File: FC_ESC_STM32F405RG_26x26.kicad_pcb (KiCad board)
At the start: 2 copper layers, 30.5 x 30.5 mm, 220 parts, among them J1 Conn_02x03_Odd_Even, J10 I2C2_UART3, J11 SD CARD, J12 UART1, J13 UART6, J14 UART4, J15 PWM, J16 MOTOR, J17 OSD, J18 Conn_01x02, J19 LED_STRIP, J2 USB_A, J20 ESC_PROG, J21 ALARM, J3 Debugger, J4 RC, J5 MOTOR, J6 MOTOR, J7 MOTOR, J8 VOL_CUR, J9 RSSI, Q1 FDS6912, Q10 FDS6912, Q11 FDS6912, Q13 FDS6912, Q2 FDS6912, Q3 FDS6912, Q4 FDS6912, Q5 FDS6912, Q6 FDS6912, Q7 FDS6912, Q8 FDS6912, Q9 FDS6912, SW1 RST, U1 TPS62822DLC, U10 EFM8BB21, U11 FD6288Q, U12 BMP280, U13 MPU-6000, U14 LM358, U15 outline, U2 TPS54560BDDA, U3 EFM8BB21, U4 FD6288Q, U5 STM32F405RGTx, U6 EFM8BB21, U7 FD6288Q, U8 EFM8BB21, U9 FD6288Q, Y1 8MHz

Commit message: update placement
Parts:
- removed Q13: FDS6912, Package_SO:SOIC-8_3.9x4.9mm_P1.27mm
- added Q12: SIZ200, Proj_footprint:ONSC-WDFN-8-511AB_V, B.Cu at (214.1, 70.3)
- C1: renamed from C11; moved to B.Cu
- C10: renamed from C38; moved to B.Cu
- C11: renamed from C28; moved to B.Cu
- C12: renamed from C39; moved to B.Cu
- C16: renamed from C13; moved to B.Cu
- C17: renamed from C40; moved to B.Cu
- C18: renamed from C16; moved to B.Cu
- C19: renamed from C41; moved to B.Cu
- C2: renamed from C36; moved to B.Cu
- C21: renamed from C17; moved to B.Cu
- C22: renamed from C42; moved to B.Cu
- C23: renamed from C29; moved to B.Cu
- C24: renamed from C43; moved to B.Cu
- C25: renamed from C30; moved to B.Cu
- C26: renamed from C44; moved to B.Cu
- C29: renamed from C31; moved to B.Cu
- C3: renamed from C12; moved to B.Cu
- C30: renamed from C45; moved to B.Cu
- C31: renamed from C32; moved to B.Cu
- C32: renamed from C46; moved to B.Cu
- C33, U4: moved to B.Cu
- C34: renamed from C47; moved to B.Cu
- C35: renamed from C34; moved to B.Cu
- C36: renamed from C48; moved to B.Cu
- C37: renamed from C35; moved to B.Cu
- C38: renamed from C49; moved to B.Cu
- C4: renamed from C37; moved to B.Cu
- C9: renamed from C27; moved to B.Cu
- D12: renamed from D3; footprint Package_TO_SOT_SMD:SOT-23-3 -> Diode_SMD:D_SOD-123F; moved to B.Cu
- D13: renamed from D11; footprint Package_TO_SOT_SMD:SOT-23-3 -> Diode_SMD:D_SOD-123F; moved to B.Cu
- D14: renamed from D4; footprint Package_TO_SOT_SMD:SOT-23-3 -> Diode_SMD:D_SOD-123F; moved to B.Cu
- D15: renamed from D12; footprint Package_TO_SOT_SMD:SOT-23-3 -> Diode_SMD:D_SOD-123F; moved to B.Cu
- D16: renamed from D7; footprint Package_TO_SOT_SMD:SOT-23-3 -> Diode_SMD:D_SOD-123F; moved to B.Cu
- D17: renamed from D13; footprint Package_TO_SOT_SMD:SOT-23-3 -> Diode_SMD:D_SOD-123F; moved to B.Cu
- D2: footprint Package_TO_SOT_SMD:SOT-23-3 -> Diode_SMD:D_SOD-123F; moved to B.Cu
- D3: renamed from D8; footprint Package_TO_SOT_SMD:SOT-23-3 -> Diode_SMD:D_SOD-123F; moved to B.Cu
- D6: renamed from D5; footprint Package_TO_SOT_SMD:SOT-23-3 -> Diode_SMD:D_SOD-123F; moved to B.Cu
- D7: renamed from D9; footprint Package_TO_SOT_SMD:SOT-23-3 -> Diode_SMD:D_SOD-123F; moved to B.Cu
- D8: renamed from D6; footprint Package_TO_SOT_SMD:SOT-23-3 -> Diode_SMD:D_SOD-123F; moved to B.Cu
- D9: renamed from D10; footprint Package_TO_SOT_SMD:SOT-23-3 -> Diode_SMD:D_SOD-123F; moved to B.Cu
- L1: footprint Inductor_SMD:L_Bourns_SRP1038C_10.0x10.0mm -> Inductor_SMD:L_Chilisin_BMRA00040420
- Q1, Q10, Q11, Q2, Q3, Q4, Q5, Q6, Q7, Q8, Q9: value FDS6912 -> SIZ200; footprint Package_SO:SOIC-8_3.9x4.9mm_P1.27mm -> Proj_footprint:ONSC-WDFN-8-511AB_V; moved to B.Cu
- R1: renamed from R8; moved to B.Cu
- R10: renamed from R23; moved to B.Cu
- R11: renamed from R47; moved to B.Cu
- R12: renamed from R48; moved to B.Cu
- R13: renamed from R24; moved to B.Cu
- R14: renamed from R49; moved to B.Cu
- R17: renamed from R12; moved to B.Cu
- R18: renamed from R13; moved to B.Cu
- R19: renamed from R50; moved to B.Cu
- R2: renamed from R43; moved to B.Cu
- R20: renamed from R51; moved to B.Cu
- R21: renamed from R19; moved to B.Cu
- R22: renamed from R20; moved to B.Cu
- R23: renamed from R52; moved to B.Cu
- R24: renamed from R53; moved to B.Cu
- R25: renamed from R21; moved to B.Cu
- R26: renamed from R54; moved to B.Cu
- R29: renamed from R14; moved to B.Cu
- R3: renamed from R9; moved to B.Cu
- R30: renamed from R15; moved to B.Cu
- R31: renamed from R55; moved to B.Cu
- R32: renamed from R56; moved to B.Cu
- R33: renamed from R18; moved to B.Cu
- R34: renamed from R16; moved to B.Cu
- R35: renamed from R57; moved to B.Cu
- R36: renamed from R58; moved to B.Cu
- R37: renamed from R17; moved to B.Cu
- R38: renamed from R59; moved to B.Cu
- R4: renamed from R10; moved to B.Cu
- R40: renamed from R26; moved to B.Cu
- R41: renamed from R60; moved to B.Cu
- R42: renamed from R27; moved to B.Cu
- R43: renamed from R28; moved to B.Cu
- R44: renamed from R29; moved to B.Cu
- R45: renamed from R61; moved to B.Cu
- R46: renamed from R62; moved to B.Cu
- R47: renamed from R63; moved to B.Cu
- R48: renamed from R30; moved to B.Cu
- R49: renamed from R31; moved to B.Cu
- R5: renamed from R11; moved to B.Cu
- R50: renamed from R64; moved to B.Cu
- R51: renamed from R65; moved to B.Cu
- R54: renamed from R32; moved to B.Cu
- R55: renamed from R66; moved to B.Cu
- R56: renamed from R33; moved to B.Cu
- R57: renamed from R34; moved to B.Cu
- R58: renamed from R67; moved to B.Cu
- R59: renamed from R68; moved to B.Cu
- R6: renamed from R44; moved to B.Cu
- R60: renamed from R35; moved to B.Cu
- R61: renamed from R36; moved to B.Cu
- R62: renamed from R69; moved to B.Cu
- R63: renamed from R70; moved to B.Cu
- R64: renamed from R37; moved to B.Cu
- R65: renamed from R71; moved to B.Cu
- R66: renamed from R38; moved to B.Cu
- R67: renamed from R39; moved to B.Cu
- R68: renamed from R72; moved to B.Cu
- R69: renamed from R73; moved to B.Cu
- R7: renamed from R45; moved to B.Cu
- R70: renamed from R40; moved to B.Cu
- R71: renamed from R41; moved to B.Cu
- R72: renamed from R74; moved to B.Cu
- R73: renamed from R75; moved to B.Cu
- R74: renamed from R42; moved to B.Cu
- R75: renamed from R76; moved to B.Cu
- R8: renamed from R46; moved to B.Cu
- R9: renamed from R22; moved to B.Cu
- U1: renamed from U3; moved to B.Cu
- U10: renamed from U11; moved to B.Cu
- U2: renamed from U8; moved to B.Cu
- U5: renamed from U9; moved to B.Cu
- U7: renamed from U6; moved to B.Cu
- U8: renamed from U10; moved to B.Cu
- U9: renamed from U7; moved to B.Cu
- Y1: footprint Crystal:Crystal_SMD_5032-4Pin_5.0x3.2mm -> Crystal:Crystal_SMD_3225-4Pin_3.2x2.5mm
- moved C16 282.4 mm to (279.4, 52.7), turned to 180 degrees
- moved C18 282.4 mm to (279.4, 60.2), turned to 180 degrees
- moved C21 282.4 mm to (279.4, 62.7), turned to 180 degrees
- moved C3 282.4 mm to (279.4, 50.1), turned to 180 degrees
- moved C11 274.4 mm to (275.4, 50.1), turned to 180 degrees
- moved R1 258.4 mm to (267.4, 52.7), turned to 180 degrees
- moved R17 258.4 mm to (267.4, 62.7), turned to 180 degrees
- moved R18 258.4 mm to (267.4, 65.2), turned to 180 degrees
- moved R29 258.4 mm to (267.4, 67.7), turned to 180 degrees
- moved R3 258.4 mm to (267.4, 55.2), turned to 180 degrees
- moved R30 258.4 mm to (267.4, 70.2), turned to 180 degrees
- moved R34 258.4 mm to (267.4, 72.7), turned to 180 degrees
- moved R37 258.4 mm to (267.4, 75.2), turned to 180 degrees
- moved R10 250.4 mm to (263.4, 52.7), turned to 180 degrees
- moved R13 250.4 mm to (263.4, 55.2), turned to 180 degrees
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- renumbered C5 to C13, C6 to C14, C7 to C15, C8 to C20, C9 to C27, C10 to C28, C52 to C39, C50 to C40, C54 to C41, C53 to C42, C26 to C43, C24 to C44, C25 to C45, C23 to C46, C22 to C47, C14 to C48, C15 to C49, C2 to C5, C18 to C50, C19 to C52, C57 to C53, C55 to C54, C56 to C55, C20 to C56, C21 to C57, C1 to C6, C3 to C7, C4 to C8, D17 to D10, D16 to D11, D14 to D4, D15 to D5, J18 to J1, J14 to J10, J15 to J11, J17 to J12, J21 to J13, J19 to J14, J4 to J15, J7 to J16, J5 to J17, J6 to J18, J16 to J19, J20 to J2, J2 to J20, J1 to J21, J8 to J4, J9 to J5, J10 to J6, J11 to J7, J12 to J8, J13 to J9, JP4 to JP1, JP1 to JP2, JP2 to JP3, JP3 to JP4, R1 to R15, R2 to R16, R3 to R27, R4 to R28, R5 to R39, R6 to R52, R7 to R53, R79 to R76, R85 to R77, R86 to R78, R77 to R79, R84 to R80, R83 to R81, R25 to R83, R78 to R84, R87 to R85, R80 to R86, R88 to R87, R89 to R88, R81 to R89, U15 to U11, U13 to U12, U12 to U13, U5 to U15, U2 to U3, U1 to U6
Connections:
- C44 pad 1: Net-(U5-PH0) -> Net-(U15-PH0)
- C45 pad 1: Net-(U5-PH1) -> Net-(U15-PH1)
- Q1 pad 2: Net-(Q1A-G1) -> Net-(Q1-G2)
- Q1 pad 3: ESC1_VS2 -> ESC1_VS1
- Q1 pad 4: Net-(Q1B-G2) -> Net-(Q1-G1)
- Q1 pad 6: V_BAT -> (no net)
- Q1 pad 7: ESC1_VS2 -> (no net)
- Q1 pad 8: ESC1_VS2 -> (no net)
- Q10 pad 6: V_BAT -> (no net)
- Q10 pad 7: ESC4_VS2 -> (no net)
- Q10 pad 8: ESC4_VS2 -> (no net)
- Q11 pad 2: Net-(Q11A-G1) -> Net-(Q11-G2)
- Q11 pad 3: ESC4_VS3 -> ESC2_VS3
- Q11 pad 4: Net-(Q11B-G2) -> Net-(Q11-G1)
- Q11 pad 6: V_BAT -> (no net)
- Q11 pad 7: ESC4_VS3 -> (no net)
- Q11 pad 8: ESC4_VS3 -> (no net)
- Q2 pad 2: Net-(Q2A-G1) -> Net-(Q2-G2)
- Q2 pad 3: ESC1_VS3 -> ESC3_VS1
- Q2 pad 4: Net-(Q2B-G2) -> Net-(Q2-G1)
- Q2 pad 6: V_BAT -> (no net)
- Q2 pad 7: ESC1_VS3 -> (no net)
- Q2 pad 8: ESC1_VS3 -> (no net)
- Q3 pad 2: Net-(Q3A-G1) -> Net-(Q3-G2)
- Q3 pad 3: ESC2_VS1 -> ESC1_VS2
- Q3 pad 4: Net-(Q3B-G2) -> Net-(Q3-G1)
- Q3 pad 6: V_BAT -> (no net)
- Q3 pad 7: ESC2_VS1 -> (no net)
- Q3 pad 8: ESC2_VS1 -> (no net)
- Q4 pad 2: Net-(Q4A-G1) -> Net-(Q4-G2)
- Q4 pad 3: ESC2_VS2 -> ESC3_VS2
- Q4 pad 4: Net-(Q4B-G2) -> Net-(Q4-G1)
- Q4 pad 6: V_BAT -> (no net)
- Q4 pad 7: ESC2_VS2 -> (no net)
- Q4 pad 8: ESC2_VS2 -> (no net)
- Q5 pad 2: Net-(Q5A-G1) -> Net-(Q5-G2)
- Q5 pad 3: ESC2_VS3 -> ESC1_VS3
- Q5 pad 4: Net-(Q5B-G2) -> Net-(Q5-G1)
- Q5 pad 6: V_BAT -> (no net)
- Q5 pad 7: ESC2_VS3 -> (no net)
- Q5 pad 8: ESC2_VS3 -> (no net)
- Q6 pad 2: Net-(Q6A-G1) -> Net-(Q6-G2)
- Q6 pad 3: ESC3_VS1 -> ESC3_VS3
- Q6 pad 4: Net-(Q6B-G2) -> Net-(Q6-G1)
- Q6 pad 6: V_BAT -> (no net)
- Q6 pad 7: ESC3_VS1 -> (no net)
- Q6 pad 8: ESC3_VS1 -> (no net)
- Q7 pad 2: Net-(Q7A-G1) -> Net-(Q7-G2)
- Q7 pad 3: ESC3_VS2 -> ESC2_VS1
- Q7 pad 4: Net-(Q7B-G2) -> Net-(Q7-G1)
- Q7 pad 6: V_BAT -> (no net)
- Q7 pad 7: ESC3_VS2 -> (no net)
- Q7 pad 8: ESC3_VS2 -> (no net)
- Q8 pad 2: Net-(Q8A-G1) -> Net-(Q8-G2)
- Q8 pad 3: ESC3_VS3 -> ESC4_VS1
- Q8 pad 4: Net-(Q8B-G2) -> Net-(Q8-G1)
- Q8 pad 6: V_BAT -> (no net)
- Q8 pad 7: ESC3_VS3 -> (no net)
- Q8 pad 8: ESC3_VS3 -> (no net)
- Q9 pad 2: Net-(Q9A-G1) -> Net-(Q9-G2)
- Q9 pad 3: ESC4_VS1 -> ESC2_VS2
- Q9 pad 4: Net-(Q9B-G2) -> Net-(Q9-G1)
- Q9 pad 6: V_BAT -> (no net)
- Q9 pad 7: ESC4_VS1 -> (no net)
- Q9 pad 8: ESC4_VS1 -> (no net)
- R17 pad 2: Net-(Q1B-G2) -> Net-(Q3-G1)
- R18 pad 2: Net-(Q1A-G1) -> Net-(Q3-G2)
- R19 pad 2: Net-(Q7B-G2) -> Net-(Q4-G1)
- R20 pad 2: Net-(Q7A-G1) -> Net-(Q4-G2)
- R29 pad 2: Net-(Q2B-G2) -> Net-(Q5-G1)
- R30 pad 2: Net-(Q2A-G1) -> Net-(Q5-G2)
- R31 pad 2: Net-(Q8B-G2) -> Net-(Q6-G1)
- R32 pad 2: Net-(Q8A-G1) -> Net-(Q6-G2)
- R4 pad 2: Net-(Q13B-G2) -> Net-(Q1-G1)
- R43 pad 2: Net-(Q3B-G2) -> Net-(Q7-G1)
- R44 pad 2: Net-(Q3A-G1) -> Net-(Q7-G2)
- R46 pad 2: Net-(Q9B-G2) -> Net-(Q8-G1)
- R47 pad 2: Net-(Q9A-G1) -> Net-(Q8-G2)
- R5 pad 2: Net-(Q13A-G1) -> Net-(Q1-G2)
- R56 pad 2: Net-(Q4B-G2) -> Net-(Q9-G1)
- R57 pad 2: Net-(Q4A-G1) -> Net-(Q9-G2)
- R66 pad 2: Net-(Q5B-G2) -> Net-(Q11-G1)
- R67 pad 2: Net-(Q5A-G1) -> Net-(Q11-G2)
- R68 pad 2: Net-(Q11B-G2) -> Net-(Q12-G1)
- R69 pad 2: Net-(Q11A-G1) -> Net-(Q12-G2)
- R7 pad 2: Net-(Q6B-G2) -> Net-(Q2-G1)
- R8 pad 2: Net-(Q6A-G1) -> Net-(Q2-G2)
- U15 pad 5: Net-(U5-PH0) -> Net-(U15-PH0)
- U15 pad 6: Net-(U5-PH1) -> Net-(U15-PH1)
- Y1 pad 1: Net-(U5-PH0) -> Net-(U15-PH1)
- Y1 pad 2: Net-(U5-PH1) -> Net-(U15-PH0)
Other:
- board size 30.5 x 30.5 mm -> 34 x 34 mm

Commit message: update placement
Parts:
- C11, C12, C13, C16, C17, C18, C19, C21, C22, C25, C26, C27, C3, C31, C32, C33, C34, C35, C36, C37, C38, C39, C4, C40, C41, C42, C43, C44, C45, C46, C47, C48, C49, C50, C51, C52, C53, C54, C55, C56, C57, C7, C8: footprint Capacitor_SMD:C_0603_1608Metric -> Capacitor_SMD:C_0402_1005Metric_Pad0.74x0.62mm_HandSolder
- J16, J17, J18, J19: footprint Connector_PinSocket_1.27mm:PinSocket_1x03_P1.27mm_Vertical -> Proj_footprint:Hirose_DF13-03P-1.25DS_1x03_P1.25mm_Horizontal; moved to B.Cu
- R1, R10, R11, R12, R13, R14, R15, R16, R17, R18, R19, R2, R20, R21, R22, R23, R24, R25, R26, R27, R28, R29, R3, R30, R31, R32, R33, R34, R35, R36, R37, R38, R39, R4, R40, R41, R42, R43, R44, R45, R46, R47, R48, R49, R5, R50, R51, R52, R53, R54, R55, R56, R57, R58, R59, R6, R60, R61, R62, R63, R64, R65, R66, R67, R68, R69, R7, R70, R71, R72, R73, R74, R75, R76, R77, R78, R79, R8, R80, R81, R82, R83, R84, R85, R86, R87, R88, R89, R9: footprint Resistor_SMD:R_0603_1608Metric -> Resistor_SMD:R_0402_1005Metric_Pad0.72x0.64mm_HandSolder
- U1, U2, U7, U8: footprint Package_DFN_QFN:SiliconLabs_QFN-20-1EP_3x3mm_P0.5mm_EP1.8x1.8mm -> Proj_footprint:QFN-20-1EP_3x3mm_P0.5mm_EP1.8x1.8mm
- U12: footprint Package_DFN_QFN:QFN-24-1EP_4x4mm_P0.5mm_EP2.15x2.15mm -> Proj_footprint:QFN-24-1EP_4x4mm_P0.5mm_EP2.15x2.15mm
- moved R41 195.9 mm to (238.7, 65.5)
- moved R45 195.9 mm to (238.7, 68.0)
- moved R73 187.6 mm to (225.4, 66.7), turned to 90 degrees
- moved R75 186.7 mm to (224.6, 69.5), turned to 90 degrees
- moved R72 183.1 mm to (223.6, 69.5), turned to -90 degrees
- moved R69 180.8 mm to (222.6, 69.5), turned to 90 degrees
- moved R68 178.7 mm to (221.7, 69.5), turned to 90 degrees
- moved R63 176.6 mm to (220.6, 66.7), turned to 90 degrees
- moved R65 175.7 mm to (219.7, 69.5), turned to 90 degrees
- moved R46 175.0 mm to (212.0, 69.5), turned to 90 degrees
- moved R62 172.2 mm to (218.8, 69.5), turned to -90 degrees
- moved R59 170.0 mm to (217.8, 69.5), turned to 90 degrees
- moved R58 167.9 mm to (216.8, 69.5), turned to 90 degrees
- moved R51 165.9 mm to (215.8, 66.7), turned to 90 degrees
- moved R55 165.0 mm to (214.9, 69.5), turned to 90 degrees
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
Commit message: update placement
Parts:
- removed the C11 at (244.1, 74.7)
- removed the C12 at (188.6, 81.3)
- removed the C25 at (159.2, 99.6)
- removed the C26 at (214.1, 40.3)
- removed the C3 at (248.2, 74.7)
- removed the C31 at (159.2, 102.1)
- removed the C32 at (214.1, 42.8)
- removed the C4 at (188.6, 78.8)
- C1, C2: footprint Capacitor_SMD:C_1210_3225Metric -> Capacitor_SMD:C_0603_1608Metric_Pad1.08x0.95mm_HandSolder
- C10: renamed from C14; footprint Capacitor_SMD:C_1210_3225Metric -> Capacitor_SMD:C_0805_2012Metric_Pad1.18x1.45mm_HandSolder
- C11: renamed from C15; footprint Capacitor_SMD:C_1210_3225Metric -> Capacitor_SMD:C_0805_2012Metric_Pad1.18x1.45mm_HandSolder
- C16: renamed from C20; footprint Capacitor_SMD:C_1210_3225Metric -> Capacitor_SMD:C_0805_2012Metric_Pad1.18x1.45mm_HandSolder
- C19: renamed from C23; footprint Capacitor_SMD:C_1210_3225Metric -> Capacitor_SMD:C_0603_1608Metric_Pad1.08x0.95mm_HandSolder
- C20: renamed from C24; footprint Capacitor_SMD:C_1210_3225Metric -> Capacitor_SMD:C_0603_1608Metric_Pad1.08x0.95mm_HandSolder
- C22: renamed from C28; footprint Capacitor_SMD:C_1210_3225Metric -> Capacitor_SMD:C_0805_2012Metric_Pad1.18x1.45mm_HandSolder
- C23: renamed from C29; value 4.7uF -> 100nF; footprint Capacitor_SMD:C_1210_3225Metric -> Capacitor_SMD:C_0402_1005Metric_Pad0.74x0.62mm_HandSolder
- C24: renamed from C30; value 4.7uF -> 100nF; footprint Capacitor_SMD:C_1210_3225Metric -> Capacitor_SMD:C_0402_1005Metric_Pad0.74x0.62mm_HandSolder
- C3: renamed from C5; footprint Capacitor_SMD:C_1210_3225Metric -> Capacitor_SMD:C_0805_2012Metric_Pad1.18x1.45mm_HandSolder
- C4: renamed from C6; footprint Capacitor_SMD:C_1210_3225Metric -> Capacitor_SMD:C_0805_2012Metric_Pad1.18x1.45mm_HandSolder
- C7: renamed from C9; value 4.7uF -> 100nF; footprint Capacitor_SMD:C_1210_3225Metric -> Capacitor_SMD:C_0402_1005Metric_Pad0.74x0.62mm_HandSolder
- C8: renamed from C10; value 4.7uF -> 100nF; footprint Capacitor_SMD:C_1210_3225Metric -> Capacitor_SMD:C_0402_1005Metric_Pad0.74x0.62mm_HandSolder
- D12, D13, D14, D15, D16, D17, D2, D3, D6, D7, D8, D9: footprint Diode_SMD:D_SOD-123F -> Diode_SMD:D_SOD-323
- moved D12 101.8 mm to (222.7, 90.6), turned to 90 degrees
- moved D14 97.1 mm to (216.8, 90.6), turned to 90 degrees
- moved D16 95.5 mm to (210.0, 90.6), turned to 90 degrees
- moved C19 83.5 mm to (215.6, 82.6), turned to 90 degrees
- moved C23 79.1 mm to (212.4, 90.6), turned to -90 degrees
- moved R54 77.8 mm to (218.3, 90.5), turned to -90 degrees
- moved R43 77.1 mm to (221.2, 90.5), turned to -90 degrees
- moved R44 76.9 mm to (220.2, 90.5), turned to -90 degrees
- moved R48 76.8 mm to (219.2, 90.5), turned to 90 degrees
- moved R42 74.4 mm to (216.8, 83.2), turned to -90 degrees
- moved R49 72.9 mm to (215.3, 93.7), turned to -90 degrees
- moved R56 72.2 mm to (215.4, 90.6), turned to -90 degrees
- moved R40 71.2 mm to (214.3, 83.2), turned to -90 degrees
- moved R57 71.2 mm to (214.4, 90.6), turned to -90 degrees
- moved R60 70.2 mm to (213.4, 90.6), turned to 90 degrees
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- renumbered C16 to C12, C17 to C13, C18 to C14, C19 to C15, C21 to C17, C22 to C18, C27 to C21, C33 to C25, C34 to C26, C35 to C27, C36 to C28, C37 to C29, C38 to C30, C39 to C31, C40 to C32, C41 to C33, C42 to C34, C43 to C35, C44 to C36, C45 to C37, C46 to C38, C47 to C39, C48 to C40, C49 to C41, C50 to C42, C51 to C43, C52 to C44, C53 to C45, C54 to C46, C55 to C47, C56 to C48, C57 to C49, C7 to C5, C8 to C6, C13 to C9

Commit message: update placement
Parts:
- removed C2, C20: 4.7uF, Capacitor_SMD:C_0603_1608Metric_Pad1.08x0.95mm_HandSolder
- removed J1: Conn_01x02, Connector_PinHeader_2.54mm:PinHeader_1x02_P2.54mm_Vertical
- added C50: 4.7uF, Capacitor_SMD:C_0603_1608Metric_Pad1.08x0.95mm_HandSolder, B.Cu at (224.2, 90.7)
- added C51: 4.7uF, Capacitor_SMD:C_0603_1608Metric_Pad1.08x0.95mm_HandSolder, B.Cu at (205.0, 88.8)
- added C52: 4.7uF, Capacitor_SMD:C_0603_1608Metric_Pad1.08x0.95mm_HandSolder, B.Cu at (226.0, 71.7)
- added C53: 4.7uF, Capacitor_SMD:C_0603_1608Metric_Pad1.08x0.95mm_HandSolder, B.Cu at (206.9, 69.8)
- added C54: 100nF, Capacitor_SMD:C_0402_1005Metric_Pad0.74x0.62mm_HandSolder, B.Cu at (219.1, 79.1)
- added C55: 100nF, Capacitor_SMD:C_0402_1005Metric_Pad0.74x0.62mm_HandSolder, B.Cu at (214.5, 76.7)
- added C56: 100nF, Capacitor_SMD:C_0402_1005Metric_Pad0.74x0.62mm_HandSolder, B.Cu at (211.9, 81.3)
- added C57: 100nF, Capacitor_SMD:C_0402_1005Metric_Pad0.74x0.62mm_HandSolder, B.Cu at (216.6, 83.8)
- added D19: SS54, Diode_SMD:D_SMB, F.Cu at (204.5, 72.2)
- added H1: VBAT, Proj_footprint:MoutingPad, F.Cu at (199.5, 73.4)
- added H2: GND, Proj_footprint:MoutingPad, F.Cu at (199.5, 70.7)
- C1, C19: footprint Capacitor_SMD:C_0603_1608Metric_Pad1.08x0.95mm_HandSolder -> Capacitor_SMD:C_1206_3216Metric_Pad1.33x1.80mm_HandSolder
- C10, C11, C3, C4: footprint Capacitor_SMD:C_0805_2012Metric_Pad1.18x1.45mm_HandSolder -> Capacitor_SMD:C_1210_3225Metric_Pad1.33x2.70mm_HandSolder
- U3: footprint Package_SO:Texas_R-PDSO-G8_EP2.95x4.9mm_Mask2.4x3.1mm_ThermalVias -> Proj_footprint:PDSO-G8_EP2.95x4.9mm_Mask2.4x3.1mm
- moved C16 193.1 mm to (144.8, 94.6)
- moved D10 193.1 mm to (169.5, 108.2)
- moved D11 193.1 mm to (169.5, 102.7)
- moved R39 193.1 mm to (141.6, 69.1)
- moved R52 193.1 mm to (141.6, 71.7)
- moved R53 193.1 mm to (141.6, 74.2)
- moved U6 193.1 mm to (138.3, 105.8)
- moved C21 193.1 mm to (129.6, 71.7)
- moved C22 193.1 mm to (150.5, 77.6)
- moved L2 193.1 mm to (150.9, 108.2)
- moved D18 184.2 mm to (205.8, 50.1)
- moved R80 184.2 mm to (210.7, 55.7)
- moved SW1 184.2 mm to (213.2, 50.7)
- moved J12 165.9 mm to (210.9, 108.6)
- moved J15 165.9 mm to (217.3, 127.4)
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
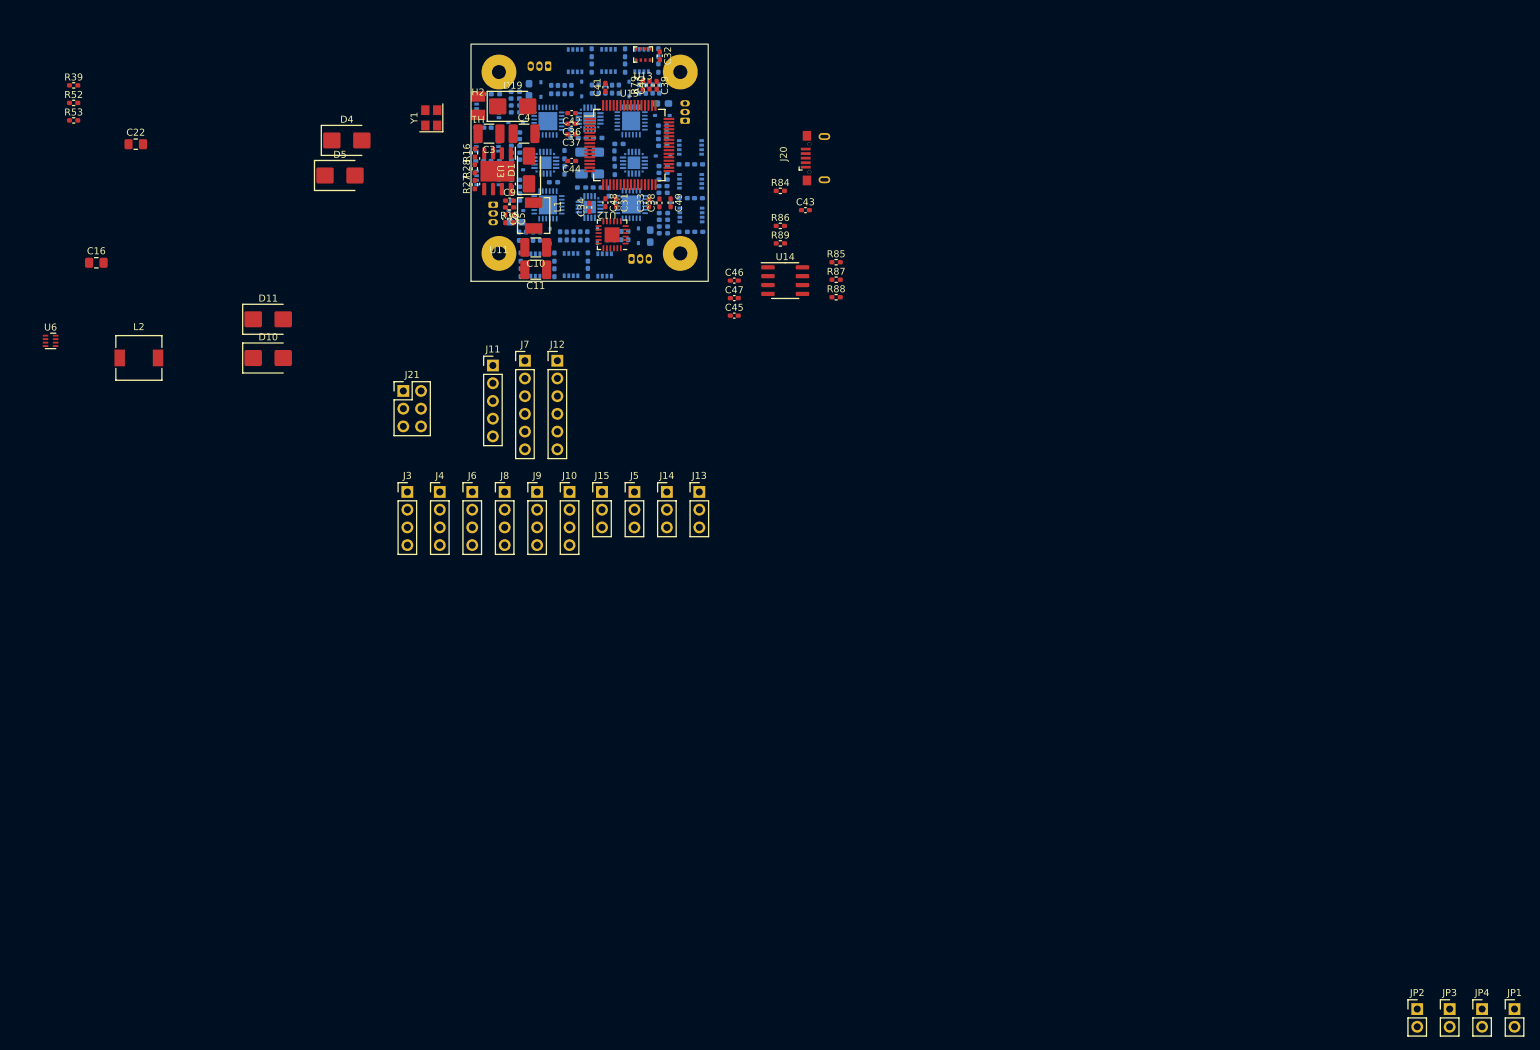
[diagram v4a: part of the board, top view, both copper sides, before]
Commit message: update placement
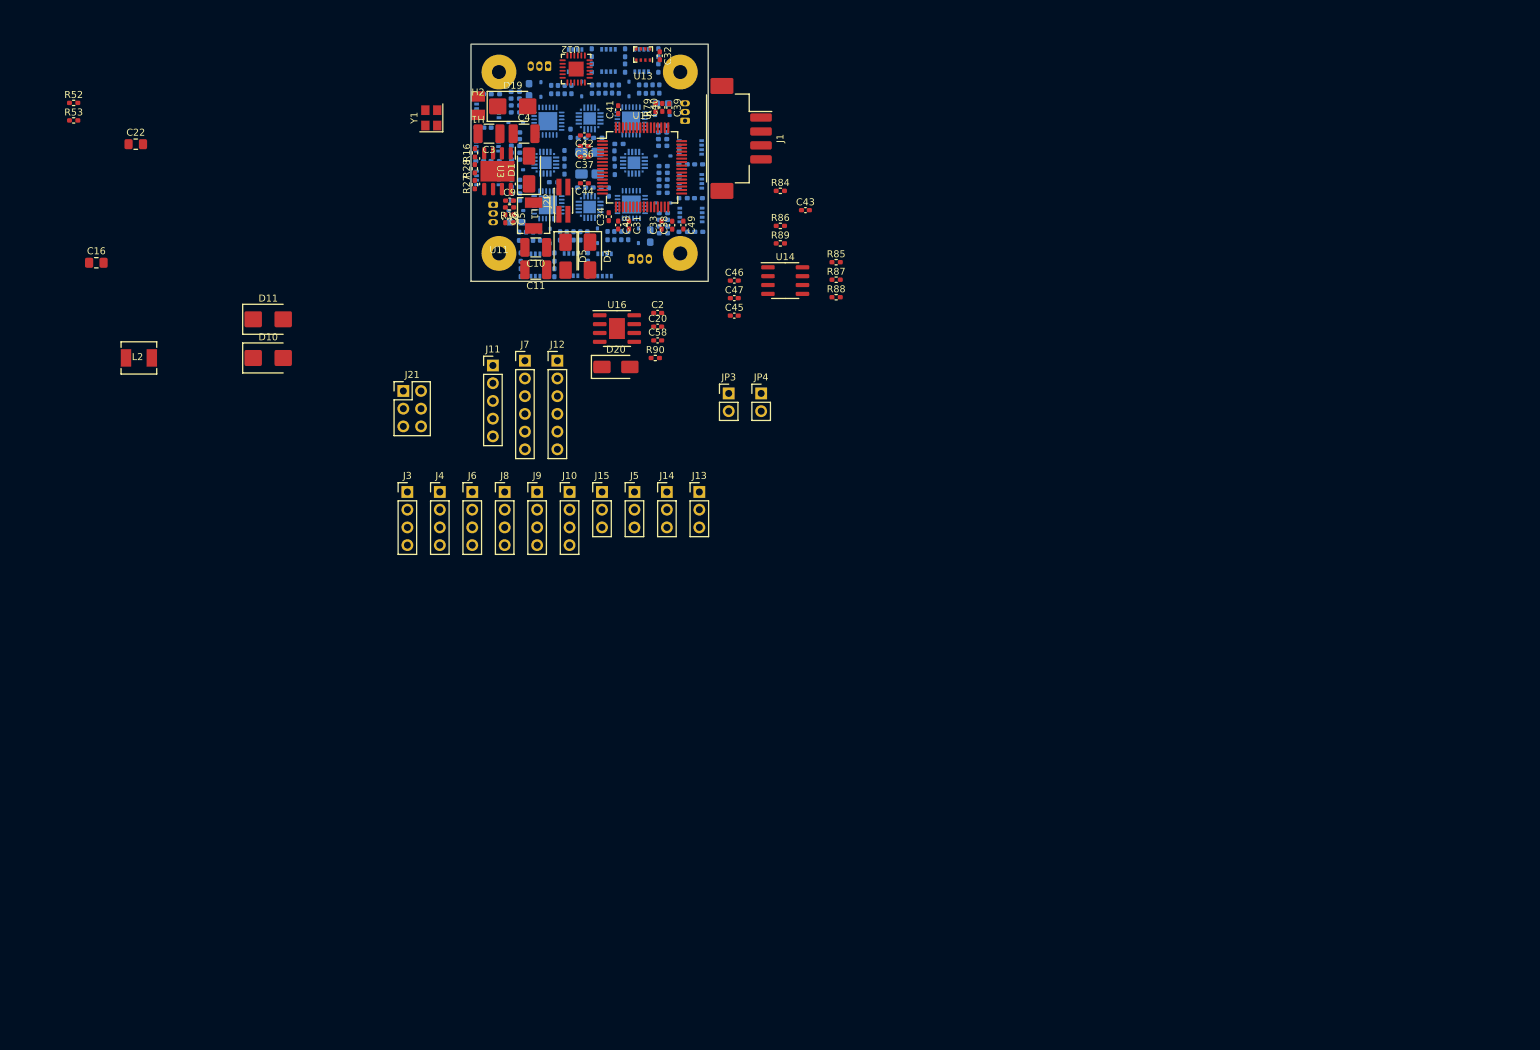
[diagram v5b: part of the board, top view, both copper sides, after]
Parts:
- removed J20: USB_A, Proj_footprint:USB_Micro-B_2P_4hole
- removed JP1: Jumper_5V, Connector_PinHeader_2.54mm:PinHeader_1x02_P2.54mm_Vertical
- removed JP2: Jumper_5V_PWR, Connector_PinHeader_2.54mm:PinHeader_1x02_P2.54mm_Vertical
- removed R39: 100k, Resistor_SMD:R_0402_1005Metric_Pad0.72x0.64mm_HandSolder
- removed U6: TPS62822DLC, Package_DFN_QFN:Texas_VSON-HR-8_1.5x2mm_P0.5mm
- added C2: 1nF, Capacitor_SMD:C_0402_1005Metric_Pad0.74x0.62mm_HandSolder, F.Cu at (225.3, 101.8)
- added C20: 10pF, Capacitor_SMD:C_0402_1005Metric_Pad0.74x0.62mm_HandSolder, F.Cu at (225.3, 103.7)
- added C58: 8.2nF, Capacitor_SMD:C_0402_1005Metric_Pad0.74x0.62mm_HandSolder, F.Cu at (225.3, 105.7)
- added D20: SS34, Diode_SMD:D_SMA, F.Cu at (219.3, 109.5)
- added J1: USB, Connector_Hirose:Hirose_DF3EA-04P-2H_1x04-1MP_P2.00mm_Horizontal, F.Cu at (237.3, 76.8)
- added J22: Conn_02x02_Odd_Even, Connector_PinHeader_1.27mm:PinHeader_2x02_P1.27mm_Vertical_SMD, F.Cu at (211.8, 85.7)
- added R90: 28.7k, Resistor_SMD:R_0402_1005Metric_Pad0.72x0.64mm_HandSolder, F.Cu at (225.0, 108.2)
- added U16: TPS54331D, Package_SO:SOIC-8-1EP_3.9x4.9mm_P1.27mm_EP2.29x3mm, F.Cu at (219.5, 104.0)
- C21: value 120pF -> 100nF
- D4, D5: value SS24 -> SS34; footprint Diode_SMD:D_SMB -> Diode_SMD:D_SMA
- L1: footprint Inductor_SMD:L_Chilisin_BMRA00040420 -> Proj_footprint:Inductor
- L2: value 470nH -> 4uH; footprint Inductor_SMD:L_6.3x6.3_H3 -> Proj_footprint:Inductor
- R16: value 274k -> 274k
- R52: value 453k -> 10k2
- R53: value 100k -> 3.24k
- moved JP3 135.9 mm to (235.5, 113.3)
- moved JP4 135.9 mm to (240.1, 113.3)
- moved D4 38.6 mm to (215.6, 93.6), turned to -90 degrees
- moved D5 34.3 mm to (212.1, 93.6), turned to -90 degrees
- moved U12 24.3 mm to (213.6, 66.8)
- moved C31 3.69 mm to (221.2, 89.2)
- moved C33 3.69 mm to (225.9, 89.2)
- moved C36 3.69 mm to (214.8, 77.8)
- moved C37 3.69 mm to (214.8, 79.4)
- moved C39 3.69 mm to (227.0, 72.3)
- moved C41 3.69 mm to (219.6, 72.6)
- moved C44 3.69 mm to (214.8, 83.2)
- moved C48 3.69 mm to (219.6, 89.2)
- moved C49 3.69 mm to (229.0, 89.2)
- moved R79 3.69 mm to (225.0, 72.3)
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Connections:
- C16 pad 1: Net-(D4-K) -> Net-(J22-Pin_4)
- C21 pad 1: Net-(D11-A) -> Net-(U16-BOOT)
- C21 pad 2: Net-(U6-FB) -> Net-(D20-K)
- L2 pad 1: Net-(U6-SW) -> Net-(D20-K)
- R52 pad 2: Net-(U6-FB) -> Net-(U16-VSENSE)
- R53 pad 1: Net-(U6-FB) -> Net-(U16-VSENSE)
